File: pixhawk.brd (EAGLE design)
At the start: 104.1 x 99.1 mm, 10 parts, among them J201 80-PIN-CARD-EDGE

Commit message: Start pixhawk board redesign
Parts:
- removed JP107: CAN, auv:DF13-4P-1.25DSA
- JP102, JP103, JP104: device auv:DF13-6P-1.25DSA -> auv:1X06
- JP105: value POWER -> PWR; device auv:DF13-6P-1.25DSA -> auv:1X06
- JP106: device auv:DF13-4P-1.25DSA -> auv:1X04
- moved JP103 80.1 mm to (74.2, 3.05), turned to 0 degrees
- moved JP101 75.7 mm to (97.8, 30.5), turned to 90 degrees
- moved JP102 44.7 mm to (55.6, 70.1), turned to 0 degrees
- moved JP104 33.4 mm to (55.1, 59.9), turned to 0 degrees
- moved JP106 20.2 mm to (91.2, 4.06), turned to 0 degrees
- moved JP105 17.6 mm to (31.0, 3.05), turned to 0 degrees
- moved U$1 13.7 mm to (52.1, 30.7), turned to 180 degrees
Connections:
- net +5V: now also JP105.1, JP105.2; no longer JP105.P$1, JP105.P$2
- net CAN_H: no longer JP107.P$2
- net CAN_L: no longer JP107.P$3
- net GND: now also JP102.6, JP103.6, JP104.6, JP105.5, JP105.6, JP106.4; no longer JP102.P$6, JP103.P$6, JP104.P$6, JP105.P$5, JP105.P$6, JP106.P$4, JP107.P$4
- net I2C_SCL: now also JP106.2; no longer JP106.P$2
- net I2C_SDA: now also JP106.3; no longer JP106.P$3
- net TELEM1_CTS: now also JP102.4; no longer JP102.P$4
- net TELEM1_RTS: now also JP102.5; no longer JP102.P$5
- net TELEM1_RX: now also JP102.3; no longer JP102.P$3
- net TELEM1_TX: now also JP102.2; no longer JP102.P$2
- net TELEM2_CTS: now also JP103.4; no longer JP103.P$4
- net TELEM2_RTS: now also JP103.5; no longer JP103.P$5
- net TELEM2_RX: now also JP103.3; no longer JP103.P$3
- net TELEM2_TX: now also JP103.2; no longer JP103.P$2
- net UART4_RX: now also JP104.3; no longer JP104.P$3
- net UART4_TX: now also JP104.2; no longer JP104.P$2
- net UART5_RX: now also JP104.5; no longer JP104.P$5
- net UART5_TX: now also JP104.4; no longer JP104.P$4
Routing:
- net PWM7: track 107.8 -> 0.00 mm, vias 1 -> 0
- net AUX2: track 107.8 -> 0.00 mm, vias 1 -> 0
- net PWM8: track 107.4 -> 0.00 mm, vias 1 -> 0
- net AUX1: track 107.4 -> 0.00 mm, vias 1 -> 0
- net PWM3: track 106.7 -> 0.00 mm, vias 1 -> 0
- net PWM1: track 106.7 -> 0.00 mm, vias 1 -> 0
- net AUX6: track 106.7 -> 0.00 mm, vias 1 -> 0
- net AUX4: track 106.7 -> 0.00 mm, vias 1 -> 0
- net PWM6: track 106.7 -> 12.7 mm
- net PWM5: track 106.7 -> 12.7 mm
- net PWM4: track 106.7 -> 12.7 mm
- net PWM2: track 106.7 -> 12.7 mm
- net AUX5: track 106.7 -> 12.7 mm
- net AUX3: track 106.7 -> 12.7 mm
- net TELEM2_TX: track 68.6 -> 0.00 mm, vias 1 -> 0
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
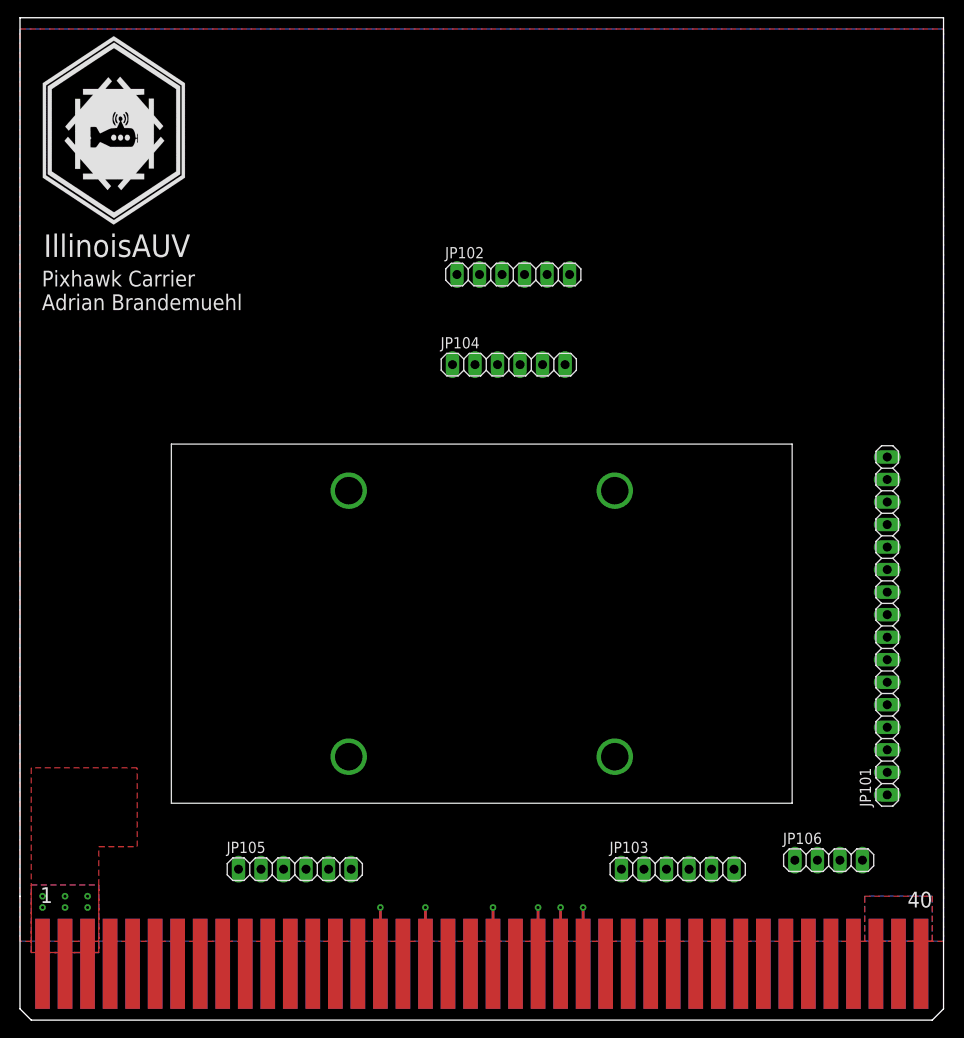
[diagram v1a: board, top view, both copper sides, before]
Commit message: adding pixhawk carrier board
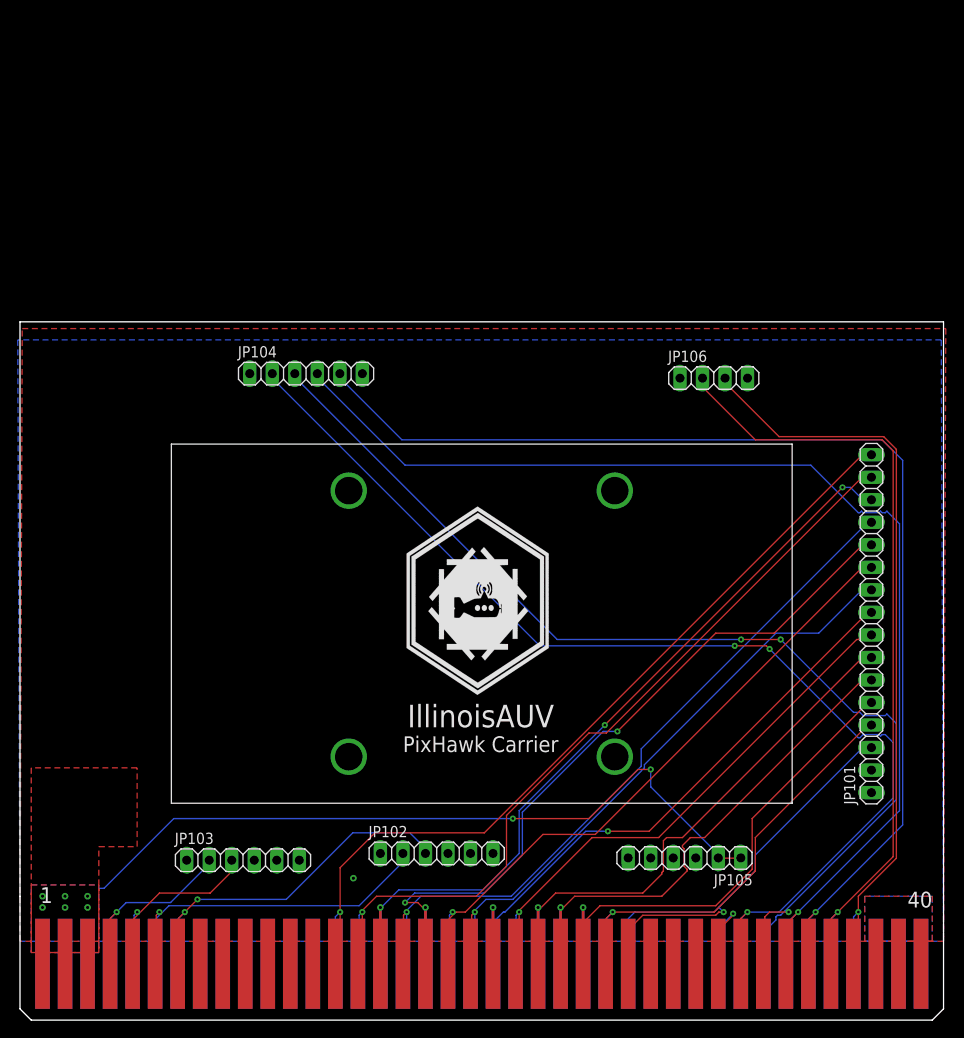
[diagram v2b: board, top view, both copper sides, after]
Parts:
- U$2: value ILLINOISAUV -> (none)
- moved U$2 67.0 mm to (52.6, 31.8)
- moved JP102 65.8 mm to (47.0, 4.83)
- moved JP106 55.9 mm to (78.2, 58.4)
- moved JP103 49.0 mm to (25.1, 4.06)
- moved JP105 44.0 mm to (74.9, 4.32), turned to 180 degrees
- moved JP104 22.9 mm to (32.3, 58.9)
- moved JP101 1.80 mm to (96.0, 30.7)
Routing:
- net UART5_RX: track 0.00 -> 135.1 mm, vias 0 -> 1
- net UART5_TX: track 0.00 -> 134.7 mm, vias 0 -> 1
- net UART4_TX: track 0.00 -> 128.3 mm, vias 0 -> 3
- net UART4_RX: track 0.00 -> 126.8 mm, vias 0 -> 3
- net AUX1: track 0.00 -> 96.3 mm, vias 0 -> 1
- net AUX2: track 0.00 -> 93.3 mm, vias 0 -> 1
- net I2C_SCL: track 0.00 -> 92.3 mm, vias 0 -> 1
- net I2C_SDA: track 0.00 -> 89.0 mm, vias 0 -> 1
- net AUX4: track 0.00 -> 83.9 mm, vias 0 -> 1
- net +5V: track 0.00 -> 83.5 mm, vias 6 -> 8
- net AUX3: track 12.7 -> 91.3 mm, vias 1 -> 3
- net AUX6: track 0.00 -> 75.5 mm, vias 0 -> 1
- net AUX5: track 12.7 -> 87.6 mm, vias 1 -> 3
- net PWM1: track 0.00 -> 72.2 mm, vias 0 -> 1
- net PWM3: track 0.00 -> 64.8 mm, vias 0 -> 1
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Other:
- board size 104.1 x 99.1 mm -> 104.1 x 64.8 mm
- board text added: "PixHawk Carrier"
- board text removed: "Pixhawk Carrier Adrian Brandemuehl"
